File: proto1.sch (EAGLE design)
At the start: 10 parts, among them U1 RASPBERRY_PICOTH, U2 GY-521MPU6050, U3 HMC5883LGY-271, U4 ESP8266_ESP-01

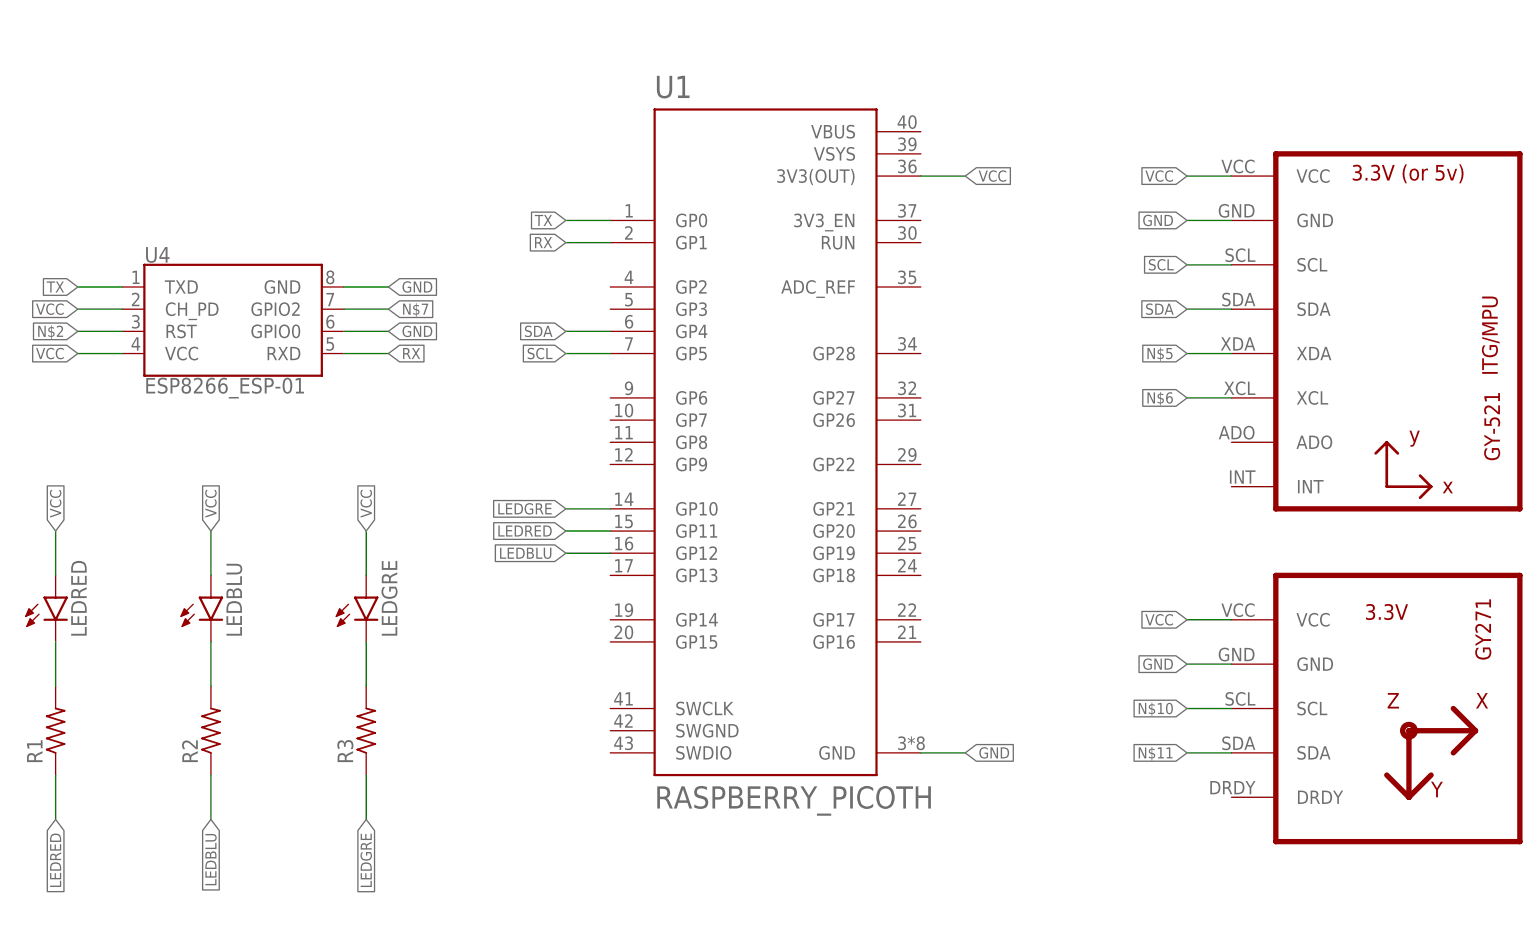
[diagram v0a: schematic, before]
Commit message: Change microcontroller
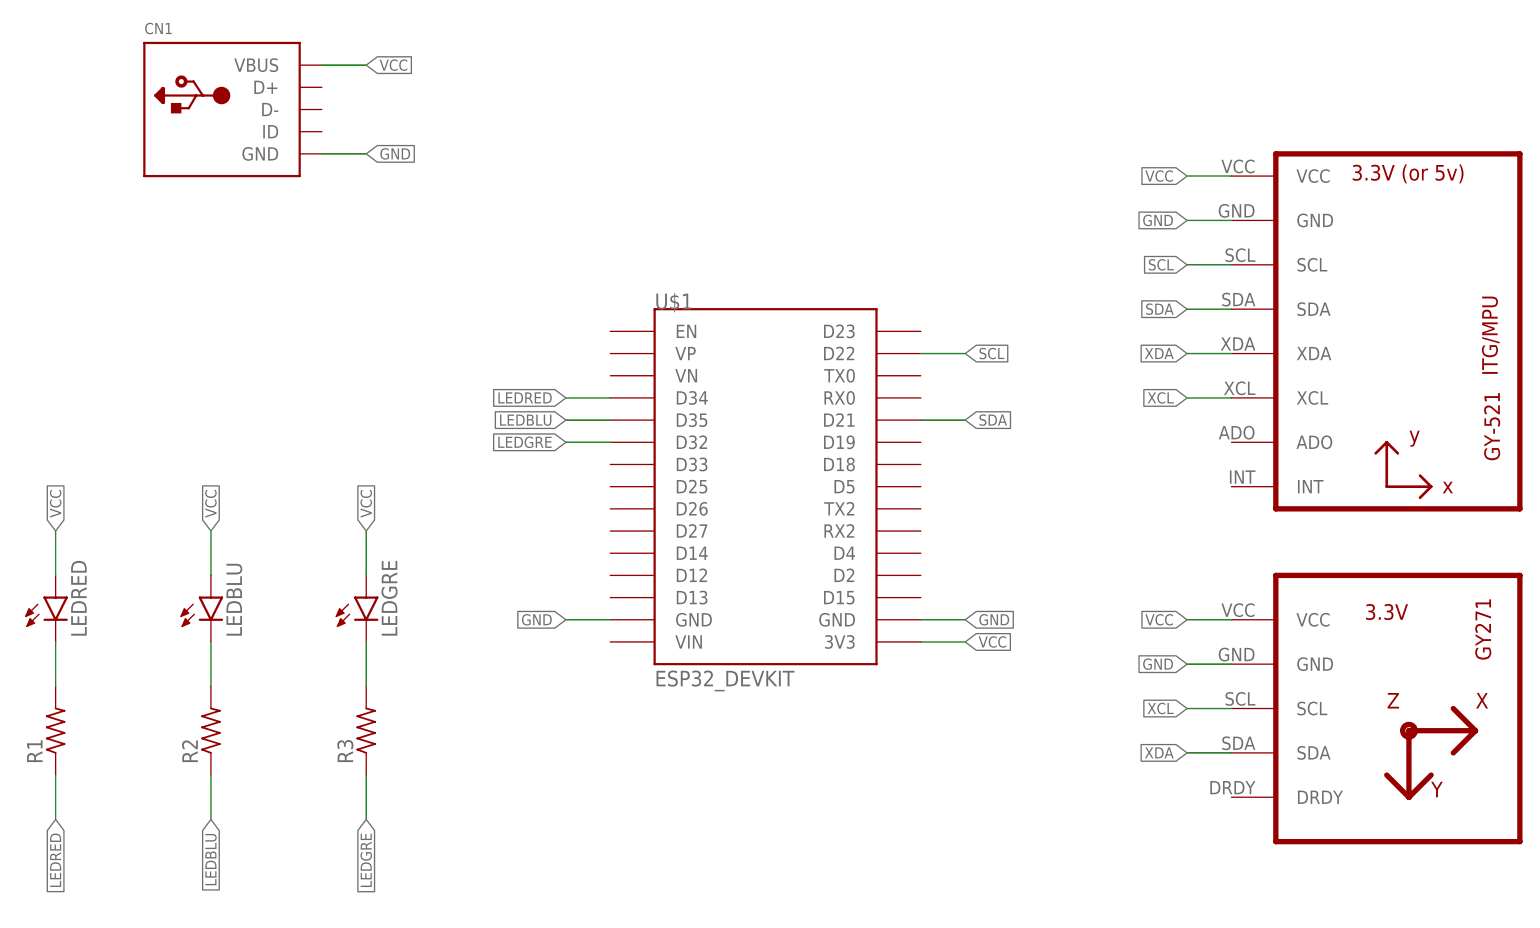
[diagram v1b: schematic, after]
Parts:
- removed U1: RASPBERRY_PICOTH, RpiPico:RASPBERRY_PICOTH
- removed U4: ESP8266_ESP-01, SparkFun-RF:ESP8266_ESP-01
- added CN1: (no value), adafruit:USBTHM
- added U$1: ESP32_DEVKIT, DOIT_ESP32_DEVKIT:ESP32_DEVKIT
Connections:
- removed net N$10: U3.SCL
- removed net N$11: U3.SDA
- removed net N$2: U4.RST
- removed net N$5: U2.XDA
- removed net N$6: U2.XCL
- removed net N$7: U4.GPIO2
- removed net RX: U1.GP1, U4.RXD
- removed net TX: U1.GP0, U4.TXD
- new net XCL: U2.XCL, U3.SCL
- new net XDA: U2.XDA, U3.SDA
- net GND: now also CN1.GND, U$1.GND@1, U$1.GND@2; no longer U1.GND, U4.GND, U4.GPIO0
- net LEDBLU: now also U$1.D35; no longer U1.GP12
- net LEDGRE: now also U$1.D32; no longer U1.GP10
- net LEDRED: now also U$1.D34; no longer U1.GP11
- net SCL: now also U$1.D22; no longer U1.GP5
- net SDA: now also U$1.D21; no longer U1.GP4
- net VCC: now also CN1.VBUS, U$1.3V3; no longer U1.3V3(OUT), U4.CH_PD, U4.VCC
